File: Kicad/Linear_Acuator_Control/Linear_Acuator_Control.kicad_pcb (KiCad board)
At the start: 2 copper layers, 93.5 x 68 mm, 21 parts, among them K1 RT42xAxx, K3 RT42xAxx, Q1 IRLB3813, Q2 IRLB3813, Q3 2N7002, Q5 2N7002, U1 ESP32-S3-WROOM

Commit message: Improving logo, solving DRCs, making renders
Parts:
- moved ? 0.32 mm to (101.7, 43.1)

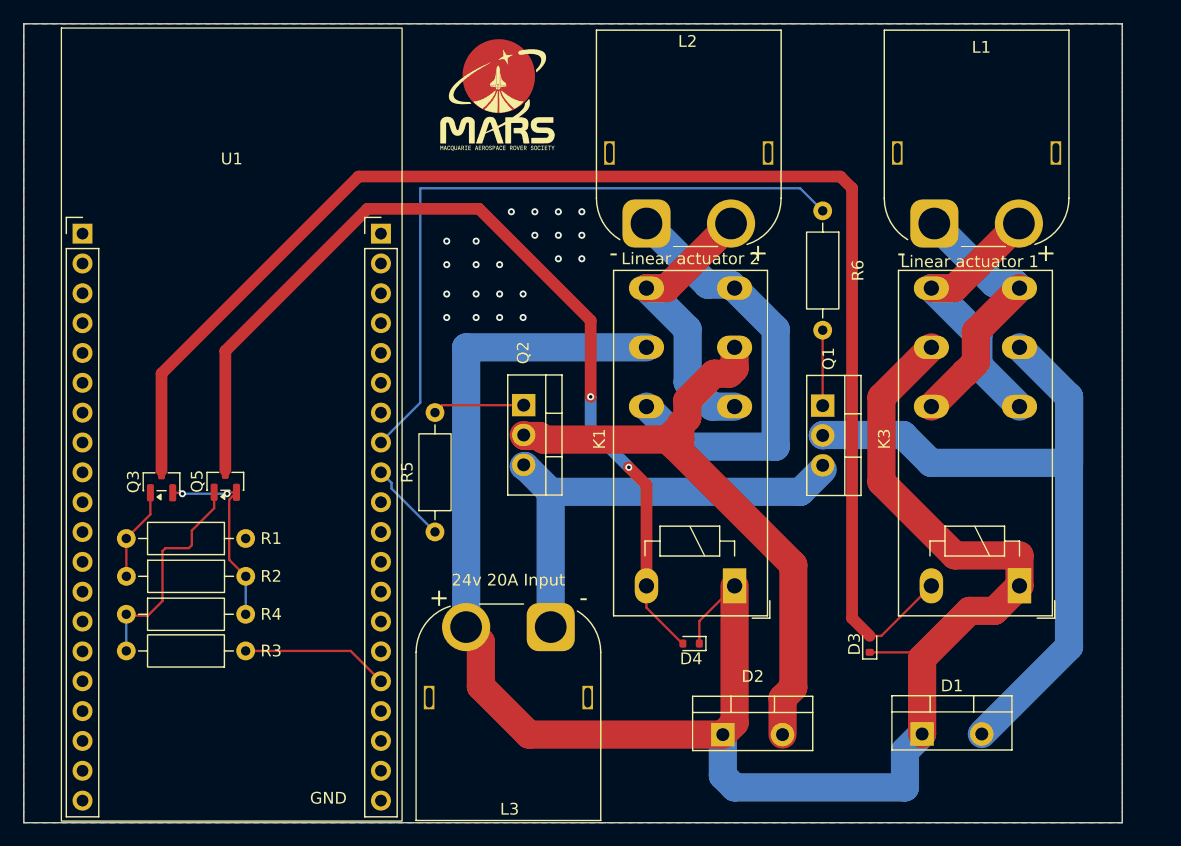
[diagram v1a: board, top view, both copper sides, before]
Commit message: resolve all non-pin spacing related DRCs
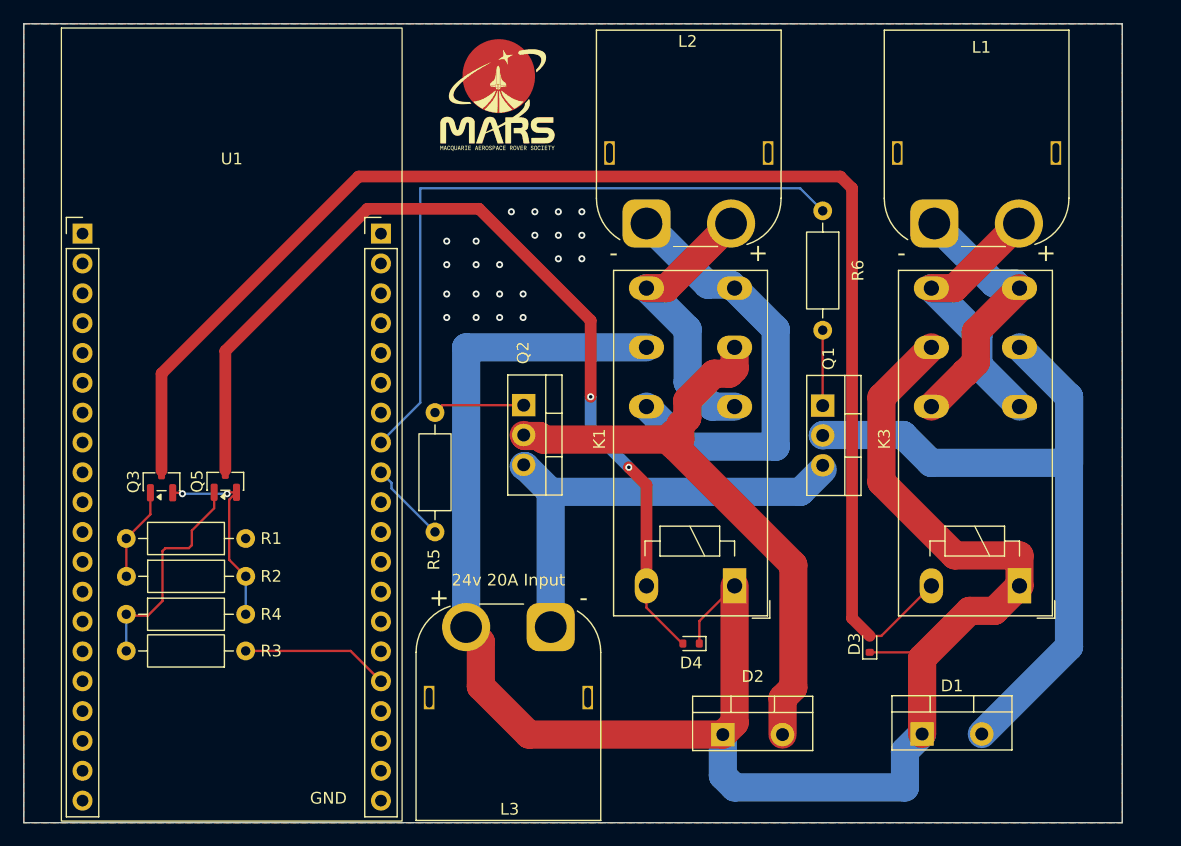
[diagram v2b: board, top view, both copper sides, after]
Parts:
- L2: value Linear actuator 2 -> Linear Actuator 2
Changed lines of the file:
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@@
 			)
 		)
-		(property "Value" "Linear actuator 2"
-			(at 3.75 3 0)
-			(layer "F.SilkS")
+		(property "Value" "Linear Actuator 2"
+			(at 4.3 -10 -0)
+			(layer "B.SilkS")
 			(effects
 				(font
@@
 					(thickness 0.15)
 				)
+				(justify mirror)
 			)
 		)
@@
 		(tags "Resistor Axial_DIN0207 series Axial Horizontal pin pitch 10.16mm 0.25W = 1/4W length 6.3mm diameter 2.5mm")
 		(property "Reference" "R5"
-			(at 5.08 -2.37 90)
+			(at -2.35 -0.1 90)
 			(layer "F.SilkS")
 			(effects
@@
 		(tags "Diode SOD523")
 		(property "Reference" "D4"
-			(at 0 -1.3 0)
+			(at 0 -1.65 0)
 			(layer "F.SilkS")
 			(effects
@@
 		)
 		(property "Value" "Linear actuator 1"
-			(at 3 3.25 0)
-			(layer "F.SilkS")
+			(at 3.6 -10 -0)
+			(layer "B.SilkS")
 			(effects
 				(font
@@
 					(thickness 0.15)
 				)
+				(justify mirror)
 			)
 		)
@@
 				(font
 					(size 1 1)
-					(thickness 0.1)
+					(thickness 0.15)
 				)
 			)
@@
 	)
 	(gr_line
+		(start 89.4 80.4)
+		(end 90.4 80.4)
+		(stroke
+			(width 0.1)
+			(type default)
+		)
+		(layer "B.SilkS")
+	)
+	(gr_line
+		(start 88.6 79)
+		(end 89.4 80.4)
+		(stroke
+			(width 0.1)
+			(type default)
+		)
+		(layer "B.SilkS")
+	)
+	(gr_line
+		(start 82.2 79)
+		(end 88.6 79)
+		(stroke
+			(width 0.1)
+			(type default)
+		)
+		(layer "B.SilkS")
+	)
+	(gr_line
 		(start 61.5 105)
 		(end 61.5 37)
@@
 			(font
 				(size 1 1)
-				(thickness 0.1)
+				(thickness 0.15)
 			)
 			(justify right bottom)
@@
 	)
 	(gr_text "39 - Speed L1"
-		(at 78.25 73 -0)
+		(at 78.25 73 0)
 		(layer "B.SilkS")
 		(effects
 			(font
 				(size 1 1)
-				(thickness 0.1)
+				(thickness 0.15)
 			)
 			(justify right bottom mirror)
@@
 	)
 	(gr_text "36 - Direction L1"
-		(at 75.75 80.75 -0)
+		(at 74.6 78.8 0)
 		(layer "B.SilkS")
 		(effects
 			(font
 				(size 1 1)
-				(thickness 0.1)
+				(thickness 0.15)
 			)
 			(justify right bottom mirror)
@@
 	)
 	(gr_text "47 - Direction L2"
-		(at 76 93.5 -0)
+		(at 76 93.5 0)
 		(layer "B.SilkS")
 		(effects
 			(font
 				(size 1 1)
-				(thickness 0.1)
+				(thickness 0.15)
 			)
 			(justify right bottom mirror)
@@
 	)
 	(gr_text "38 - Speed L2"
-		(at 78.25 76 -0)
+		(at 78.25 76 0)
 		(layer "B.SilkS")
 		(effects
 			(font
 				(size 1 1)
-				(thickness 0.1)
+				(thickness 0.15)
 			)
 			(justify right bottom mirror)

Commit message: fixing other DRC related problems
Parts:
- moved U1 0.18 mm to (79.2, 45.6)

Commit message: smoothing capacitors
transients hate to see me coming
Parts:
- added C1: 1000u, Capacitor_THT:CP_Radial_D12.5mm_P5.00mm, F.Cu at (133.5, 60.5)
- added C2: 1000u, Capacitor_THT:CP_Radial_D12.5mm_P5.00mm, F.Cu at (100.5, 62.0)
- R5: footprint Resistor_THT:R_Axial_DIN0207_L6.3mm_D2.5mm_P10.16mm_Horizontal -> Resistor_SMD:R_0201_0603Metric
- R6: footprint Resistor_THT:R_Axial_DIN0207_L6.3mm_D2.5mm_P10.16mm_Horizontal -> Resistor_SMD:R_0201_0603Metric; moved to B.Cu
- moved R5 5.58 mm to (94.6, 75.0)
- moved L1 5.50 mm to (144.5, 54.0)
- moved K3 5.29 mm to (151.5, 85.5)
- moved D2 4.46 mm to (116.6, 98.2)
- moved D1 3.85 mm to (141.8, 97.2)
- moved D3 3.00 mm to (136.5, 89.8)
- moved Q1 1.61 mm to (131.1, 69.5)
- moved R6 0.58 mm to (129.5, 53.5)
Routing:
- net +24V: track 162.9 -> 188.8 mm
- net Net-(Q1-G): track 6.42 -> 16.7 mm
- net Net-(D3-A): track 120.1 -> 127.6 mm
- net Net-(Q2-G): track 7.81 -> 13.5 mm
- net Speed L2: track 6.98 -> 2.97 mm
- net Net-(D1-A): track 65.4 -> 68.8 mm
- net Net-(D2-A): track 54.4 -> 57.2 mm
- net Net-(L1-Pin_2): track 22.9 -> 24.9 mm
- net GND: vias 24 -> 27
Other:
- board size 93.5 x 68 mm -> 96.5 x 68 mm
